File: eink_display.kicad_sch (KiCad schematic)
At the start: 8 parts, among them J1 FH34SRJ-24S-0.5SH (50)

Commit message: small stuff
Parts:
- added C10, C8: 1uF/50V, symbol Device:C
- added C9: 4.7uF/50V, symbol Device:C
- added D1, D2, D3: MBR0530, Diode_SMD:D_SOD-123, symbol Diode:MBR0530
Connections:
- net GND: now also C10.1, C8.1, D2.1 (K)
- net VGH: now also C10.2, D3.1 (K)
- net VGL: now also C8.2, D1.2 (A)
- new net: C9.1, D3.2 (A)
- new net: C9.2, D1.1 (K), D2.2 (A)

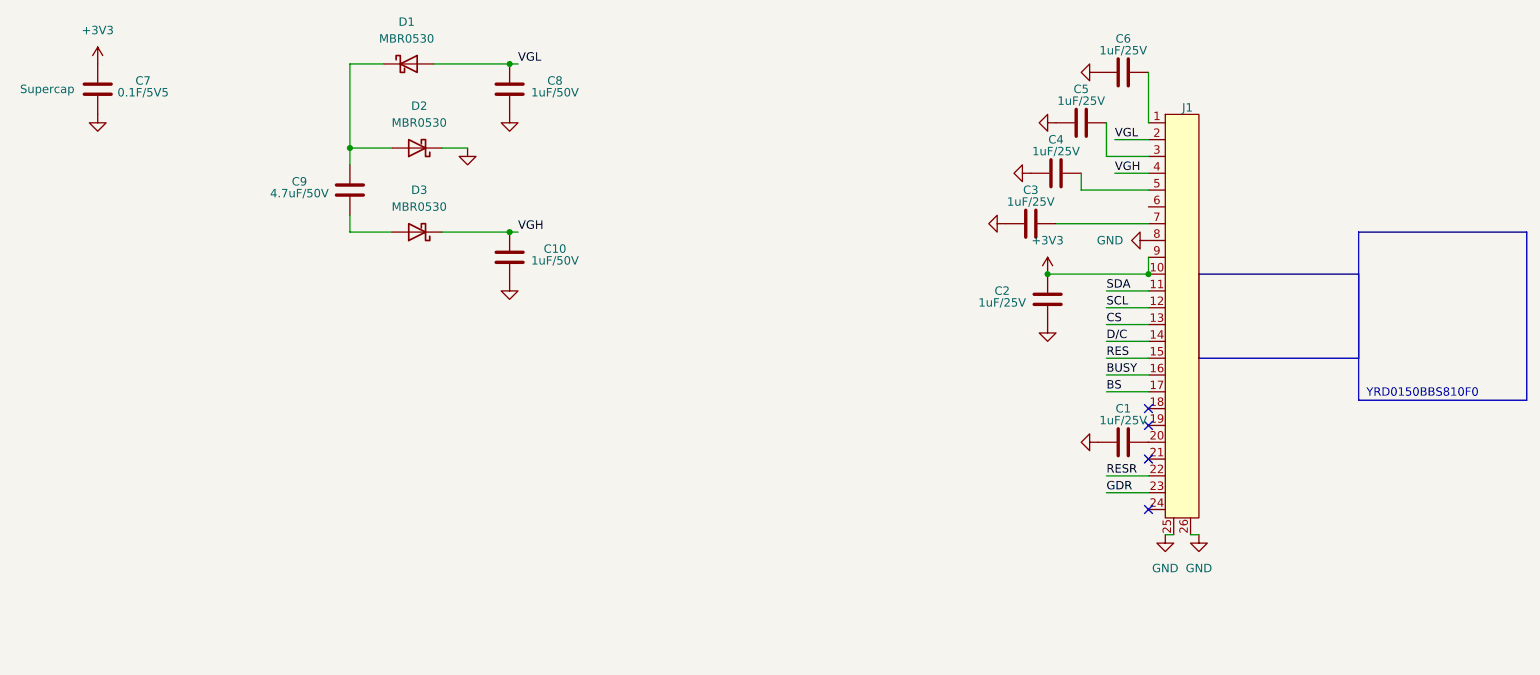
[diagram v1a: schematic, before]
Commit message: done the eink display schematic
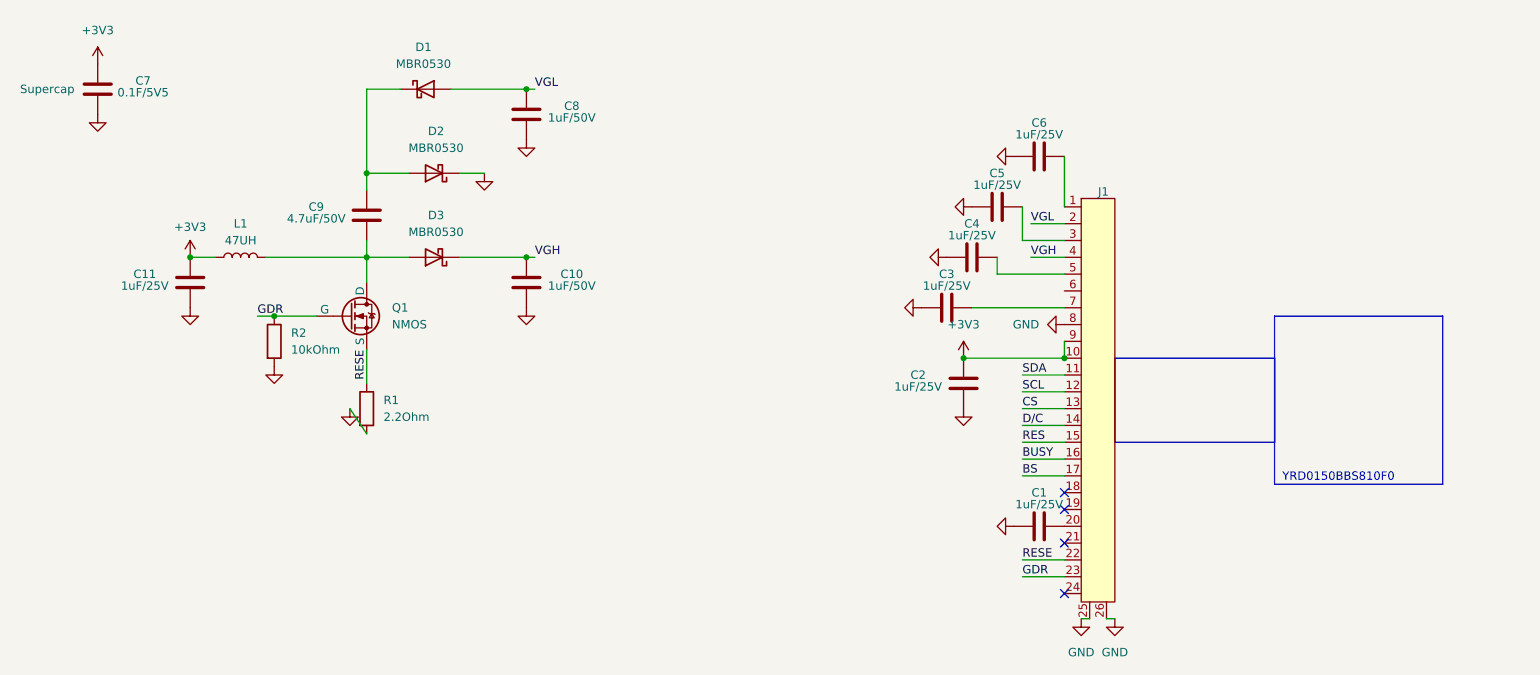
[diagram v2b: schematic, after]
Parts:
- added C11: 1uF/25V, symbol Device:C
- added L1: 47UH, symbol Device:L
- added Q1: NMOS, symbol Simulation_SPICE:NMOS
- added R1: 2.2Ohm, symbol Device:R
- added R2: 10kOhm, symbol Device:R
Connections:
- net +3V3: now also C11.2, L1.1
- net GDR: now also Q1.2 (G), R2.1
- net GND: now also C11.1, R1.2, R2.2
- net at C9.1, D3.2 (A): now also L1.2, Q1.1 (D)
- net RESR renamed RESE
- net RESE: now also Q1.3 (S), R1.1
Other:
- moved on the sheet: C1, C10, C2, C3, C4, C5, C6, C8, C9, D1, D2, D3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

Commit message: done the power sch for the mcu
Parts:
- Q1: value NMOS -> SI1304BdL
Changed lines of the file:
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@@
-	(wire
-		(pts
-			(xy 78.74 93.98) (xy 76.2 90.17)
-		)
-		(stroke
-			(width 0)
-			(type default)
-		)
-	)
 	(wire
 		(pts
@@
 			)
 		)
-		(property "Value" "NMOS"
+		(property "Value" "SI1304BdL"
 			(at 82.55 77.4699 0)
 			(show_name no)
@@
 	(symbol
 		(lib_id "power:GND")
-		(at 76.2 90.17 0)
+		(at 78.74 93.98 0)
 		(unit 1)
 		(body_style 1)
@@
 		(fields_autoplaced yes)
 		(property "Reference" "#PWR016"
-			(at 76.2 96.52 0)
+			(at 78.74 100.33 0)
 			(hide yes)
 			(show_name no)
@@
 		)
 		(property "Value" "GND"
-			(at 76.2 95.25 0)
+			(at 78.74 99.06 0)
 			(hide yes)
 			(show_name no)
@@
 		)
 		(property "Footprint" ""
-			(at 76.2 90.17 0)
+			(at 78.74 93.98 0)
 			(hide yes)
 			(show_name no)
@@
 		)
 		(property "Datasheet" ""
-			(at 76.2 90.17 0)
+			(at 78.74 93.98 0)
 			(hide yes)
 			(show_name no)
@@
 		)
 		(property "Description" "Power symbol creates a global label with name \"GND\" , ground"
-			(at 76.2 90.17 0)
-			(hide yes)
-			(show_name no)
+			(at 78.74 93.98 0)
+			(hide yes)
+			(show_name no)

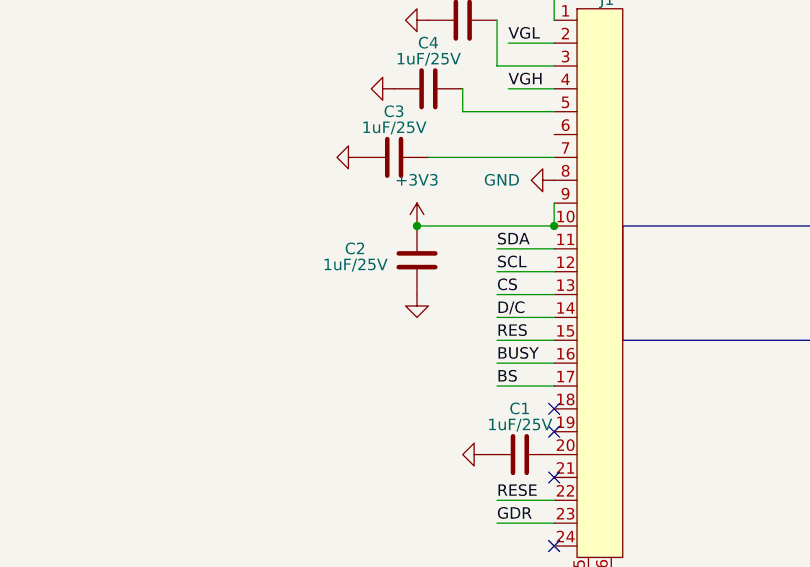
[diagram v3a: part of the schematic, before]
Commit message: changed eink display labels
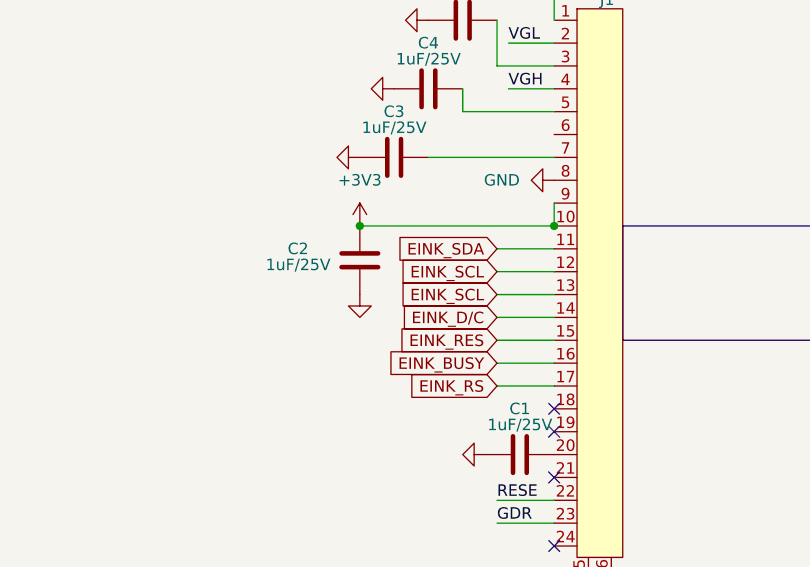
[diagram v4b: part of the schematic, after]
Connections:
- net SCL is gone; now on net EINK_SCL: J1.12
- net BS renamed EINK_RS
- net BUSY renamed EINK_BUSY
- net CS renamed EINK_SCL
- net D/C renamed EINK_D/C
- net RES renamed EINK_RES
- net SDA renamed EINK_SDA
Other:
- moved on the sheet: C2
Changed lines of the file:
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@@
 	)
 	(junction
-		(at 168.91 82.55)
+		(at 162.56 82.55)
 		(diameter 0)
 		(color 0 0 0 0)
@@
 	(wire
 		(pts
-			(xy 168.91 82.55) (xy 184.15 82.55)
-		)
-		(stroke
-			(width 0)
-			(type default)
-		)
-	)
-	(wire
-		(pts
 			(xy 179.07 67.31) (xy 184.15 67.31)
 		)
@@
 	(wire
 		(pts
-			(xy 102.87 41.91) (xy 91.44 41.91)
+			(xy 162.56 82.55) (xy 184.15 82.55)
 		)
 		(stroke
@@
 		)
 	)
-	(label "BUSY"
-		(at 177.8 97.79 0)
-		(effects
-			(font
-				(size 1.27 1.27)
-			)
-			(justify left bottom)
+	(wire
+		(pts
+			(xy 102.87 41.91) (xy 91.44 41.91)
+		)
+		(stroke
+			(width 0)
+			(type default)
 		)
 	)
@@
 		)
 	)
-	(label "CS"
-		(at 177.8 90.17 0)
+	(label "VGH"
+		(at 179.07 67.31 0)
 		(effects
 			(font
@@
 		)
 	)
-	(label "RES"
-		(at 177.8 95.25 0)
+	(label "VGL"
+		(at 179.07 62.23 0)
 		(effects
 			(font
@@
 		)
 	)
-	(label "BS"
-		(at 177.8 100.33 0)
+	(label "RESE"
+		(at 78.74 81.28 270)
 		(effects
 			(font
 				(size 1.27 1.27)
 			)
-			(justify left bottom)
+			(justify right bottom)
 		)
 	)
-	(label "SCL"
-		(at 177.8 87.63 0)
+	(label "VGL"
+		(at 104.14 41.91 0)
 		(effects
 			(font
@@
 		)
 	)
-	(label "VGH"
-		(at 179.07 67.31 0)
+	(global_label "EINK_RES"
+		(shape input)
+		(at 177.8 95.25 180)
+		(fields_autoplaced yes)
 		(effects
 			(font
 				(size 1.27 1.27)
 			)
-			(justify left bottom)
+			(justify right)
+		)
+		(property "Intersheetrefs" "${INTERSHEET_REFS}"
+			(at 165.8644 95.25 0)
+			(hide yes)
+			(show_name no)
+			(do_not_autoplace no)
+			(effects
+				(font
+					(size 1.27 1.27)
+				)
+				(justify right)
+			)
 		)
 	)
-	(label "VGL"
-		(at 179.07 62.23 0)
+	(global_label "EINK_SCL"
+		(shape input)
+		(at 177.8 90.17 180)
+		(fields_autoplaced yes)
 		(effects
 			(font
 				(size 1.27 1.27)
 			)
-			(justify left bottom)
+			(justify right)
+		)
+		(property "Intersheetrefs" "${INTERSHEET_REFS}"
+			(at 165.9853 90.17 0)
+			(hide yes)
+			(show_name no)
+			(do_not_autoplace no)
+			(effects
+				(font
+					(size 1.27 1.27)
+				)
+				(justify right)
+			)
 		)
 	)
-	(label "SDA"
-		(at 177.8 85.09 0)
+	(global_label "EINK_BUSY"
+		(shape input)
+		(at 177.8 97.79 180)
+		(fields_autoplaced yes)
 		(effects
 			(font
 				(size 1.27 1.27)
 			)
-			(justify left bottom)
+			(justify right)
+		)
+		(property "Intersheetrefs" "${INTERSHEET_REFS}"
+			(at 164.5943 97.79 0)
+			(hide yes)
+			(show_name no)
+			(do_not_autoplace no)
+			(effects
+				(font
+					(size 1.27 1.27)
+				)
+				(justify right)
+			)
 		)
 	)
-	(label "RESE"
-		(at 78.74 81.28 270)
+	(global_label "EINK_RS"
+		(shape input)
+		(at 177.8 100.33 180)
+		(fields_autoplaced yes)
 		(effects
 			(font
 				(size 1.27 1.27)
 			)
-			(justify right bottom)
+			(justify right)
+		)
+		(property "Intersheetrefs" "${INTERSHEET_REFS}"
+			(at 167.0134 100.33 0)
+			(hide yes)
+			(show_name no)
+			(do_not_autoplace no)
+			(effects
+				(font
+					(size 1.27 1.27)
+				)
+				(justify right)
+			)
 		)
 	)
-	(label "VGL"
-		(at 104.14 41.91 0)
+	(global_label "EINK_D{slash}C"
+		(shape input)
+		(at 177.8 92.71 180)
+		(fields_autoplaced yes)
 		(effects
 			(font
 				(size 1.27 1.27)
 			)
-			(justify left bottom)
+			(justify right)
+		)
+		(property "Intersheetrefs" "${INTERSHEET_REFS}"
+			(at 165.6224 92.71 0)
+			(hide yes)
+			(show_name no)
+			(do_not_autoplace no)
+			(effects
+				(font
+					(size 1.27 1.27)
+				)
+				(justify right)
+			)
 		)
 	)
-	(label "D{slash}C"
-		(at 177.8 92.71 0)
+	(global_label "EINK_SCL"
+		(shape input)
+		(at 177.8 87.63 180)
+		(fields_autoplaced yes)
 		(effects
 			(font
 				(size 1.27 1.27)
 			)
-			(justify left bottom)
+			(justify right)
+		)
+		(property "Intersheetrefs" "${INTERSHEET_REFS}"
+			(at 165.9853 87.63 0)
+			(hide yes)
+			(show_name no)
+			(do_not_autoplace no)
+			(effects
+				(font
+					(size 1.27 1.27)
+				)
+				(justify right)
+			)
+		)
+	)
+	(global_label "EINK_SDA"
+		(shape input)
+		(at 177.8 85.09 180)
+		(fields_autoplaced yes)
+		(effects
+			(font
+				(size 1.27 1.27)
+			)
+			(justify right)
+		)
+		(property "Intersheetrefs" "${INTERSHEET_REFS}"
+			(at 165.9248 85.09 0)
+			(hide yes)
+			(show_name no)
+			(do_not_autoplace no)
+			(effects
+				(font
+					(size 1.27 1.27)
+				)
+				(justify right)
+			)
 		)
 	)
@@
 	(symbol
 		(lib_id "Device:C")
-		(at 168.91 86.36 180)
+		(at 162.56 86.36 180)
 		(unit 1)
 		(body_style 1)
@@
 		(dnp no)
 		(property "Reference" "C2"
-			(at 162.052 85.09 0)
+			(at 155.702 85.09 0)
 			(show_name no)
 			(do_not_autoplace no)
@@
 		)
 		(property "Value" "1uF/25V"
-			(at 162.052 86.868 0)
+			(at 155.702 86.868 0)
 			(show_name no)
 			(do_not_autoplace no)
@@
 		)
 		(property "Footprint" ""
-			(at 167.9448 82.55 0)
+			(at 161.5948 82.55 0)
 			(hide yes)
 			(show_name no)
@@
 		)
 		(property "Datasheet" ""
-			(at 168.91 86.36 0)
+			(at 162.56 86.36 0)
 			(hide yes)
 			(show_name no)
@@
 		)
 		(property "Description" "Unpolarized capacitor"
-			(at 168.91 86.36 0)
+			(at 162.56 86.36 0)
 			(hide yes)
 			(show_name no)
@@
 	(symbol
 		(lib_id "power:GND")
-		(at 168.91 90.17 0)
+		(at 162.56 90.17 0)
 		(unit 1)
 		(body_style 1)
@@
 		(fields_autoplaced yes)
 		(property "Reference" "#PWR04"
-			(at 168.91 96.52 0)
+			(at 162.56 96.52 0)
 			(hide yes)
 			(show_name no)
@@
 		)
 		(property "Value" "GND"
-			(at 168.91 95.25 0)
+			(at 162.56 95.25 0)
 			(hide yes)
 			(show_name no)
@@
 		)
 		(property "Footprint" ""
-			(at 168.91 90.17 0)
+			(at 162.56 90.17 0)
 			(hide yes)
 			(show_name no)
@@
 		)
 		(property "Datasheet" ""
-			(at 168.91 90.17 0)
+			(at 162.56 90.17 0)
 			(hide yes)
 			(show_name no)
@@
 		)
 		(property "Description" "Power symbol creates a global label with name \"GND\" , ground"
-			(at 168.91 90.17 0)
+			(at 162.56 90.17 0)
 			(hide yes)
 			(show_name no)
@@
 	(symbol
 		(lib_id "power:+3V3")
-		(at 168.91 82.55 0)
+		(at 162.56 82.55 0)
 		(unit 1)
 		(body_style 1)
@@
 		(fields_autoplaced yes)
 		(property "Reference" "#PWR012"
-			(at 168.91 86.36 0)
+			(at 162.56 86.36 0)
 			(hide yes)
 			(show_name no)
@@
 		)
 		(property "Value" "+3V3"
-			(at 168.91 77.47 0)
+			(at 162.56 77.47 0)
 			(show_name no)
 			(do_not_autoplace no)
@@
 		)
 		(property "Footprint" ""
-			(at 168.91 82.55 0)
+			(at 162.56 82.55 0)
 			(hide yes)
 			(show_name no)
@@
 		)
 		(property "Datasheet" ""
-			(at 168.91 82.55 0)
+			(at 162.56 82.55 0)
 			(hide yes)
 			(show_name no)
@@
 		)
 		(property "Description" "Power symbol creates a global label with name \"+3V3\""
-			(at 168.91 82.55 0)
+			(at 162.56 82.55 0)
 			(hide yes)
 			(show_name no)
